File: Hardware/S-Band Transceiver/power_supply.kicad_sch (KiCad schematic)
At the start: 0 parts

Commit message: Updates to power supply schematic
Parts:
- added U14: AP2127K-3.3, Package_TO_SOT_SMD:SOT-23-5, symbol Regulator_Linear:AP2127K-3.3
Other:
- note added: "Power requirements ADF4351: 3.3V, 27+36+80+26 mA = 169 mA ADL5380: 5V, 245 mA 2 x TSS-53LNB3+: 3V, 42 mA each 2 x ADL5906: 5V, 68 mA PE44820: 3.3V, 1 mA DAT-31A+: 3.3V, 1 mA"
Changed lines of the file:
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@@
 		(rev "v1.0")
 	)
+	(text "Power requirements\nADF4351: 3.3V, 27+36+80+26 mA = 169 mA\nADL5380: 5V, 245 mA\n2 x TSS-53LNB3+: 3V, 42 mA each\n2 x ADL5906: 5V, 68 mA\nPE44820: 3.3V, 1 mA\nDAT-31A+: 3.3V, 1 mA\n\n"
+		(exclude_from_sim no)
+		(at 41.91 30.226 0)
+		(effects
+			(font
+				(size 1.27 1.27)
+			)
+			(justify left)
+		)
+	)
+	(symbol
+		(lib_id "Regulator_Linear:AP2127K-3.3")
+		(at 87.63 44.45 0)
+		(unit 1)
+		(exclude_from_sim no)
+		(in_bom yes)
+		(on_board yes)
+		(dnp no)
+		(fields_autoplaced yes)
+		(property "Reference" "U14"
+			(at 87.63 35.56 0)
+			(effects
+				(font
+					(size 1.27 1.27)
+				)
+			)
+		)
+		(property "Value" "AP2127K-3.3"
+			(at 87.63 38.1 0)
+			(effects
+				(font
+					(size 1.27 1.27)
+				)
+			)
+		)
+		(property "Footprint" "Package_TO_SOT_SMD:SOT-23-5"
+			(at 87.63 36.195 0)
+			(effects
+				(font
+					(size 1.27 1.27)
+				)
+				(hide yes)
+			)
+		)
+		(property "Datasheet" "https://www.diodes.com/assets/Datasheets/AP2127.pdf"
+			(at 87.63 41.91 0)
+			(effects
+				(font
+					(size 1.27 1.27)
+				)
+				(hide yes)
+			)
+		)
+		(property "Description" "300mA low dropout linear regulator, shutdown pin, 2.5V-6V input voltage, 3.3V fixed positive output, SOT-23-5"
+			(at 87.63 44.45 0)
+			(effects
+				(font
+					(size 1.27 1.27)
+				)
+				(hide yes)
+			)
+		)
+		(pin "1"
+		)
+		(pin "2"
+		)
+		(pin "5"
+		)
+		(pin "3"
+		)
+		(pin "4"
+		)
+		(instances
+			(project "S-Band Transceiver"
+				(path "/811f57cf-e3df-4fba-aff9-353adc85299e/39233606-ce53-49cf-9f32-d543f22663a6"
+					(reference "U14")
+					(unit 1)
+				)
+			)
+		)
+	)
 )

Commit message: Changes to schematic
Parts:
- removed U14: AP2127K-3.3, Package_TO_SOT_SMD:SOT-23-5, symbol Regulator_Linear:AP2127K-3.3
- added C40: 10uF, symbol Device:C_Polarized_Small_US
- added C41: 22uF, symbol Device:C_Polarized_Small_US
- added U14: AZ1117-3.3, Package_TO_SOT_SMD:SOT-223-3_TabPin2, symbol Regulator_Linear:AZ1117-3.3
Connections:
- new net +3V3A: C41.1, U14.2 (VO)
- new net +5V: C40.1, U14.3 (VI)
- new net GND: C40.2, C41.2, U14.1 (GND)
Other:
- note added: "B0505XT-2WR3"

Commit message: Updating schematic
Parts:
- added C4: 10uF, symbol Device:C_Polarized_Small_US
- added C5: 4.7uF, symbol Device:C_Polarized_Small_US
- added U2: IES0105S05-H, symbol _tim-DC_DC:IES0105S05-H
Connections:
- net +5V: now also C5.1, U2.2 (+Vin)
- net GND: now also C4.1, C5.2, U2.1 (-Vin), U2.5 (+Vout)
- new net -5V: C4.2, U2.4 (-Vout)
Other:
- note added: "1 Amp Max"
- note added: "200mA Max"
- note added: "B0505XT-2WR3 or IES0105S05-H"
- note removed: "B0505XT-2WR3"

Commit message: Updates to schematic
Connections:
- net +3V3A renamed +3.3VA
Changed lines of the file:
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@@
 	(wire
 		(pts
-			(xy 101.6 45.72) (xy 101.6 48.26)
+			(xy 101.6 44.45) (xy 101.6 48.26)
 		)
 		(stroke
@@
 		)
 	)
-	(global_label "+3V3A"
-		(shape input)
-		(at 101.6 45.72 90)
+	(symbol
+		(lib_id "power:+3.3VA")
+		(at 101.6 44.45 0)
+		(unit 1)
+		(exclude_from_sim no)
+		(in_bom yes)
+		(on_board yes)
+		(dnp no)
 		(fields_autoplaced yes)
-		(effects
-			(font
-				(size 1.27 1.27)
-			)
-			(justify left)
-		)
-		(property "Intersheetrefs" "${INTERSHEET_REFS}"
-			(at 101.6 36.5662 90)
+		(property "Reference" "#PWR0123"
+			(at 101.6 48.26 0)
 			(effects
 				(font
 					(size 1.27 1.27)
 				)
-				(justify left)
 				(hide yes)
 			)
 		)
+		(property "Value" "+3.3VA"
+			(at 101.6 39.37 0)
+			(effects
+				(font
+					(size 1.27 1.27)
+				)
+			)
+		)
+		(property "Footprint" ""
+			(at 101.6 44.45 0)
+			(effects
+				(font
+					(size 1.27 1.27)
+				)
+				(hide yes)
+			)
+		)
+		(property "Datasheet" ""
+			(at 101.6 44.45 0)
+			(effects
+				(font
+					(size 1.27 1.27)
+				)
+				(hide yes)
+			)
+		)
+		(property "Description" "Power symbol creates a global label with name \"+3.3VA\""
+			(at 101.6 44.45 0)
+			(effects
+				(font
+					(size 1.27 1.27)
+				)
+				(hide yes)
+			)
+		)
+		(pin "1"
+		)
+		(instances
+			(project "S-Band Transceiver"
+				(path "/811f57cf-e3df-4fba-aff9-353adc85299e/39233606-ce53-49cf-9f32-d543f22663a6"
+					(reference "#PWR0123")
+					(unit 1)
+				)
+			)
+		)

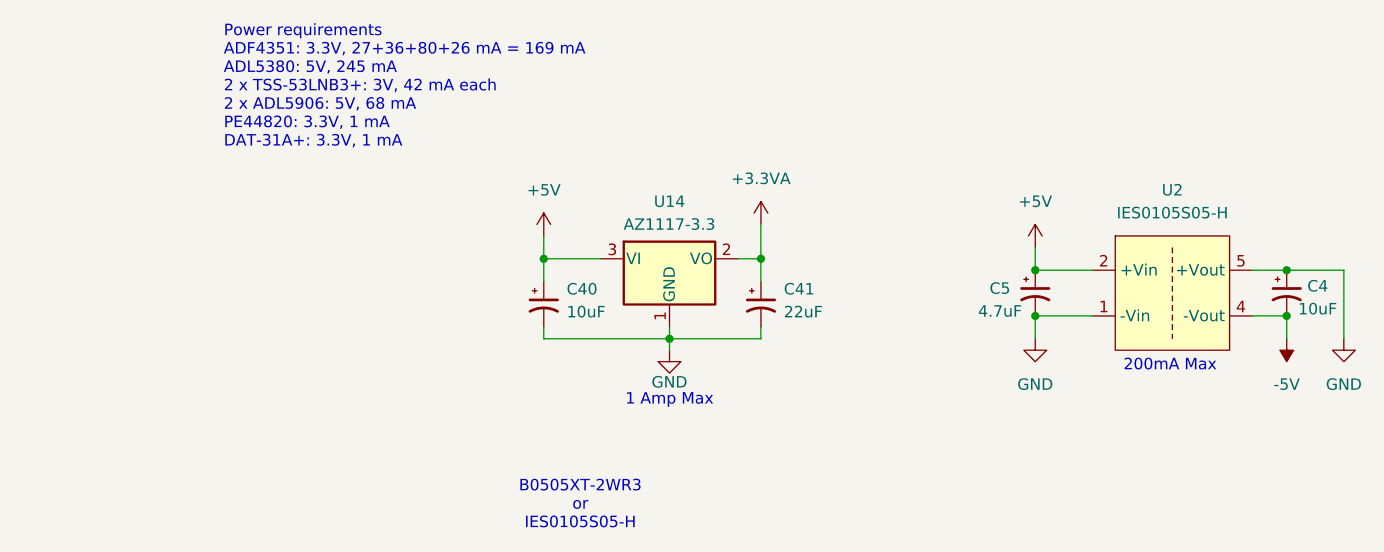
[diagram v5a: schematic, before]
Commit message: Updates to Schematic
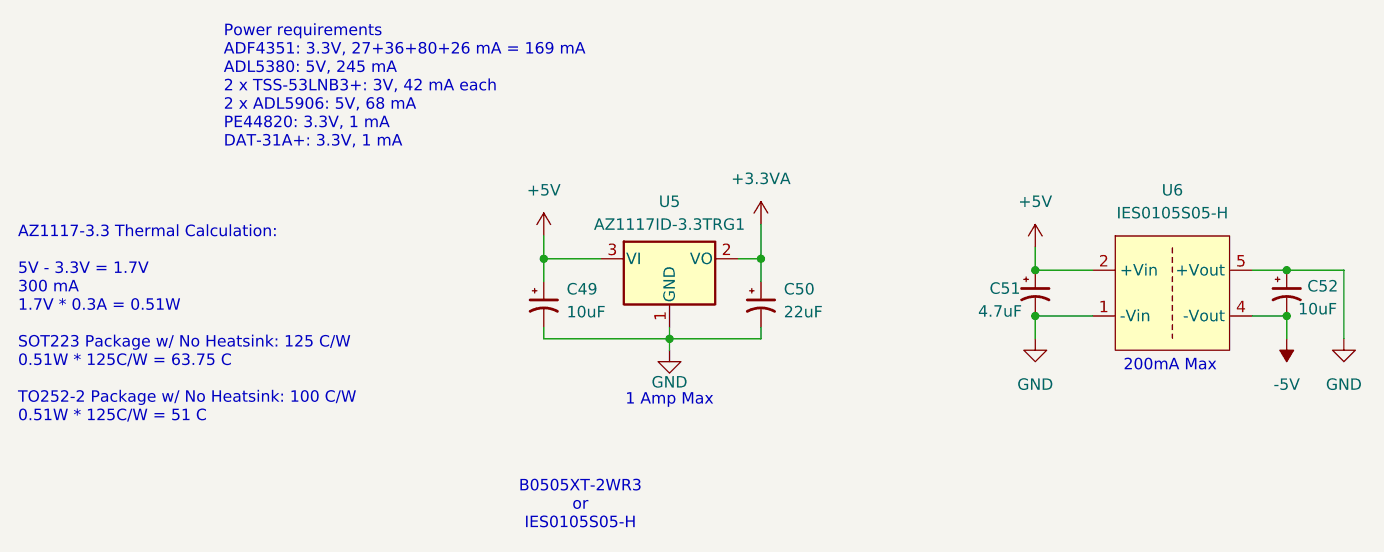
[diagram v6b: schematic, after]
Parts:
- U5: renamed from U14; value AZ1117-3.3 -> AZ1117ID-3.3TRG1; footprint Package_TO_SOT_SMD:SOT-223-3_TabPin2 -> Package_TO_SOT_SMD:TO-252-2; Digikey (none) -> AZ1117ID-3.3TRG1-ND
- U6: renamed from U2; footprint (none) -> _tim-DC-DC:IES0105S05-H; Digikey (none) -> 1470-IES0105S05-H-ND
- renumbered C40 to C49, C41 to C50, C5 to C51, C4 to C52
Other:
- note added: "AZ1117-3.3 Thermal Calculation: 5V - 3.3V = 1.7V 300 mA 1.7V * 0.3A = 0.51W SOT223 Package w/ No Heatsink: 125 C/W 0.51W * 125C/W = 63.75 C TO252-2 Package w/ No Heatsink: 100 C/W 0.51W * 125C/W = 51 C"
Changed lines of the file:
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@@
+		)
+	)
+	(text "AZ1117-3.3 Thermal Calculation:\n\n5V - 3.3V = 1.7V\n300 mA\n1.7V * 0.3A = 0.51W\n\nSOT223 Package w/ No Heatsink: 125 C/W\n0.51W * 125C/W = 63.75 C\n\nTO252-2 Package w/ No Heatsink: 100 C/W\n0.51W * 125C/W = 51 C\n"
+		(exclude_from_sim no)
+		(at 19.05 55.626 0)
+		(effects
+			(font
+				(size 1.27 1.27)
+			)
+			(justify left)
 		)
 	)
@@
 		(dnp no)
 		(fields_autoplaced yes)
-		(property "Reference" "#PWR0123"
+		(property "Reference" "#PWR067"
 			(at 101.6 48.26 0)
 			(effects
@@
 			(project "S-Band Transceiver"
 				(path "/811f57cf-e3df-4fba-aff9-353adc85299e/39233606-ce53-49cf-9f32-d543f22663a6"
-					(reference "#PWR0123")
+					(reference "#PWR067")
 					(unit 1)
 				)
@@
 		(dnp no)
 		(fields_autoplaced yes)
-		(property "Reference" "U2"
+		(property "Reference" "U6"
 			(at 147.32 40.64 0)
 			(effects
@@
 			)
 		)
-		(property "Footprint" ""
+		(property "Footprint" "_tim-DC-DC:IES0105S05-H"
 			(at 147.32 52.07 0)
 			(effects
@@
 			)
 		)
+		(property "Digikey" "1470-IES0105S05-H-ND"
+			(at 147.32 52.07 0)
+			(effects
+				(font
+					(size 1.27 1.27)
+				)
+				(hide yes)
+			)
+		)
 		(pin "5"
 		)
@@
 			(project "S-Band Transceiver"
 				(path "/811f57cf-e3df-4fba-aff9-353adc85299e/39233606-ce53-49cf-9f32-d543f22663a6"
-					(reference "U2")
+					(reference "U6")
 					(unit 1)
 				)
@@
 		(dnp no)
 		(fields_autoplaced yes)
-		(property "Reference" "U14"
+		(property "Reference" "U5"
 			(at 91.44 41.91 0)
 			(effects
@@
 			)
 		)
-		(property "Value" "AZ1117-3.3"
+		(property "Value" "AZ1117ID-3.3TRG1"
 			(at 91.44 44.45 0)
 			(effects
@@
 			)
 		)
-		(property "Footprint" "Package_TO_SOT_SMD:SOT-223-3_TabPin2"
+		(property "Footprint" "Package_TO_SOT_SMD:TO-252-2"
 			(at 91.44 41.91 0)
 			(effects
@@
 			)
 		)
+		(property "Digikey" "AZ1117ID-3.3TRG1-ND"
+			(at 91.44 48.26 0)
+			(effects
+				(font
+					(size 1.27 1.27)
+				)
+				(hide yes)
+			)
+		)
 		(pin "2"
 		)
@@
 			(project "S-Band Transceiver"
 				(path "/811f57cf-e3df-4fba-aff9-353adc85299e/39233606-ce53-49cf-9f32-d543f22663a6"
-					(reference "U14")
+					(reference "U5")
 					(unit 1)
 				)
@@
 		(dnp no)
 		(fields_autoplaced yes)
-		(property "Reference" "#PWR0106"
+		(property "Reference" "#PWR068"
 			(at 132.08 50.8 0)
 			(effects
@@
 			(project "S-Band Transceiver"
 				(path "/811f57cf-e3df-4fba-aff9-353adc85299e/39233606-ce53-49cf-9f32-d543f22663a6"
-					(reference "#PWR0106")
+					(reference "#PWR068")
 					(unit 1)
 				)
@@
 		(dnp no)
 		(fields_autoplaced yes)
-		(property "Reference" "#PWR062"
+		(property "Reference" "#PWR065"
 			(at 77.47 49.53 0)
 			(effects
@@
 			(project "S-Band Transceiver"
 				(path "/811f57cf-e3df-4fba-aff9-353adc85299e/39233606-ce53-49cf-9f32-d543f22663a6"
-					(reference "#PWR062")
+					(reference "#PWR065")
 					(unit 1)
 				)
@@
 		(on_board yes)
 		(dnp no)
-		(property "Reference" "#PWR061"
+		(property "Reference" "#PWR066"
 			(at 91.44 64.77 0)
 			(effects
@@
 			(project "S-Band Transceiver"
 				(path "/811f57cf-e3df-4fba-aff9-353adc85299e/39233606-ce53-49cf-9f32-d543f22663a6"
-					(reference "#PWR061")
+					(reference "#PWR066")
 					(unit 1)
 				)
@@
 		(dnp no)
 		(fields_autoplaced yes)
-		(property "Reference" "#PWR0105"
+		(property "Reference" "#PWR069"
 			(at 132.08 63.5 0)
 			(effects
@@
 			(project "S-Band Transceiver"
 				(path "/811f57cf-e3df-4fba-aff9-353adc85299e/39233606-ce53-49cf-9f32-d543f22663a6"
-					(reference "#PWR0105")
+					(reference "#PWR069")
 					(unit 1)
 				)
@@
 		(on_board yes)
 		(dnp no)
-		(property "Reference" "C5"
+		(property "Reference" "C51"
 			(at 127 51.562 0)
 			(effects
@@
 			(project "S-Band Transceiver"
 				(path "/811f57cf-e3df-4fba-aff9-353adc85299e/39233606-ce53-49cf-9f32-d543f22663a6"
-					(reference "C5")
+					(reference "C51")
 					(unit 1)
 				)
@@
 		(dnp no)
 		(fields_autoplaced yes)
-		(property "Reference" "C40"
+		(property "Reference" "C49"
 			(at 80.01 51.6381 0)
 			(effects
@@
 			(project "S-Band Transceiver"
 				(path "/811f57cf-e3df-4fba-aff9-353adc85299e/39233606-ce53-49cf-9f32-d543f22663a6"
-					(reference "C40")
+					(reference "C49")
 					(unit 1)
 				)
@@
 		(dnp no)
 		(fields_autoplaced yes)
-		(property "Reference" "#PWR0104"
+		(property "Reference" "#PWR070"
 			(at 160.02 53.34 0)
 			(effects
@@
 			(project "S-Band Transceiver"
 				(path "/811f57cf-e3df-4fba-aff9-353adc85299e/39233606-ce53-49cf-9f32-d543f22663a6"
-					(reference "#PWR0104")
+					(reference "#PWR070")
 					(unit 1)
 				)
@@
 		(dnp no)
 		(fields_autoplaced yes)
-		(property "Reference" "C41"
+		(property "Reference" "C50"
 			(at 104.14 51.6381 0)
 			(effects
@@
 			(project "S-Band Transceiver"
 				(path "/811f57cf-e3df-4fba-aff9-353adc85299e/39233606-ce53-49cf-9f32-d543f22663a6"
-					(reference "C41")
+					(reference "C50")
 					(unit 1)
 				)
@@
 		(dnp no)
 		(fields_autoplaced yes)
-		(property "Reference" "#PWR0103"
+		(property "Reference" "#PWR071"
 			(at 166.37 63.5 0)
 			(effects
@@
 			(project "S-Band Transceiver"
 				(path "/811f57cf-e3df-4fba-aff9-353adc85299e/39233606-ce53-49cf-9f32-d543f22663a6"
-					(reference "#PWR0103")
+					(reference "#PWR071")
 					(unit 1)
 				)
@@
 		(on_board yes)
 		(dnp no)
-		(property "Reference" "C4"
+		(property "Reference" "C52"
 			(at 162.306 51.308 0)
 			(effects
@@
 			(project "S-Band Transceiver"
 				(path "/811f57cf-e3df-4fba-aff9-353adc85299e/39233606-ce53-49cf-9f32-d543f22663a6"
-					(reference "C4")
-					(unit 1)
-				)
+					(reference "C52")
+					(unit 1)
+				)

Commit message: Finished assigning footprints and starting board layout
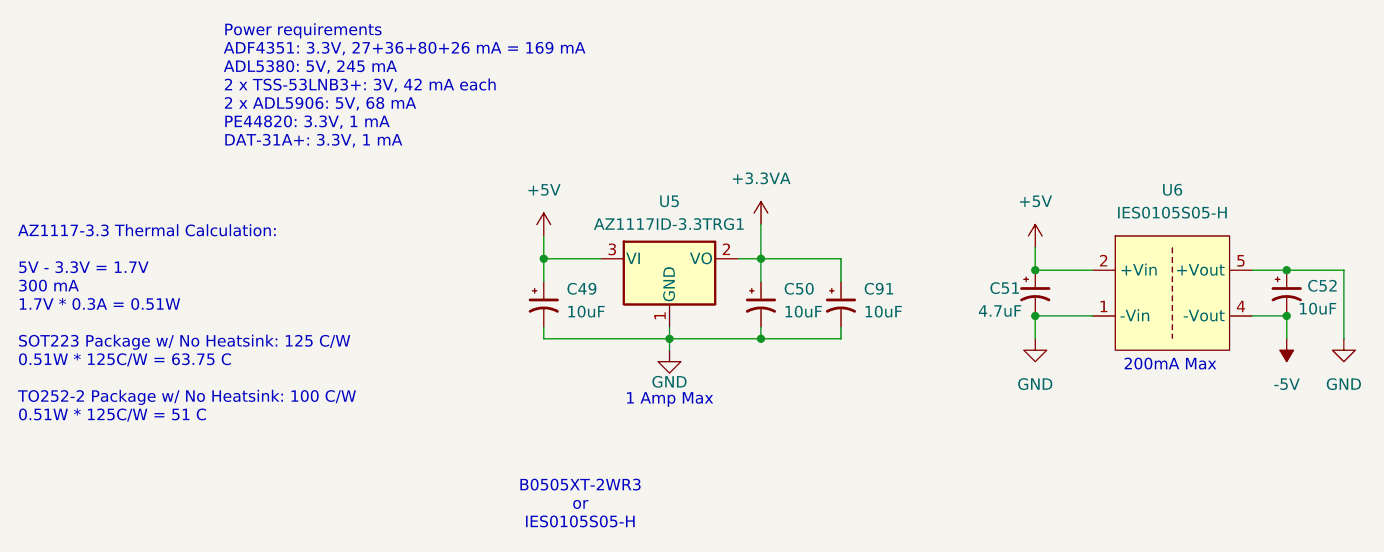
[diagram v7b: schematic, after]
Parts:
- added C91: 10uF, Capacitor_Tantalum_SMD:CP_EIA-3216-18_Kemet-A, symbol Device:C_Polarized_Small_US
- C49, C51, C52: footprint (none) -> Capacitor_Tantalum_SMD:CP_EIA-3216-18_Kemet-A
- C50: value 22uF -> 10uF; footprint (none) -> Capacitor_Tantalum_SMD:CP_EIA-3216-18_Kemet-A
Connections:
- net +3.3VA: now also C91.1
- net GND: now also C91.2
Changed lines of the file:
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@@
+	)
+	(junction
+		(at 101.6 57.15)
+		(diameter 0)
+		(color 0 0 0 0)
 	)
 	(junction
@@
 	(wire
 		(pts
+			(xy 110.49 48.26) (xy 101.6 48.26)
+		)
+		(stroke
+			(width 0)
+			(type default)
+		)
+	)
+	(wire
+		(pts
 			(xy 156.21 49.53) (xy 160.02 49.53)
 		)
@@
 	(wire
 		(pts
+			(xy 110.49 55.88) (xy 110.49 57.15)
+		)
+		(stroke
+			(width 0)
+			(type default)
+		)
+	)
+	(wire
+		(pts
 			(xy 77.47 48.26) (xy 77.47 50.8)
 		)
@@
 		(pts
 			(xy 101.6 55.88) (xy 101.6 57.15)
+		)
+		(stroke
+			(width 0)
+			(type default)
+		)
+	)
+	(wire
+		(pts
+			(xy 110.49 50.8) (xy 110.49 48.26)
+		)
+		(stroke
+			(width 0)
+			(type default)
+		)
+	)
+	(wire
+		(pts
+			(xy 110.49 57.15) (xy 101.6 57.15)
 		)
 		(stroke
@@
 			)
 		)
-		(property "Footprint" ""
+		(property "Footprint" "Capacitor_Tantalum_SMD:CP_EIA-3216-18_Kemet-A"
 			(at 132.08 52.07 0)
 			(effects
@@
 	(symbol
 		(lib_id "Device:C_Polarized_Small_US")
+		(at 101.6 53.34 0)
+		(unit 1)
+		(exclude_from_sim no)
+		(in_bom yes)
+		(on_board yes)
+		(dnp no)
+		(fields_autoplaced yes)
+		(property "Reference" "C50"
+			(at 104.14 51.6381 0)
+			(effects
+				(font
+					(size 1.27 1.27)
+				)
+				(justify left)
+			)
+		)
+		(property "Value" "10uF"
+			(at 104.14 54.1781 0)
+			(effects
+				(font
+					(size 1.27 1.27)
+				)
+				(justify left)
+			)
+		)
+		(property "Footprint" "Capacitor_Tantalum_SMD:CP_EIA-3216-18_Kemet-A"
+			(at 101.6 53.34 0)
+			(effects
+				(font
+					(size 1.27 1.27)
+				)
+				(hide yes)
+			)
+		)
+		(property "Datasheet" "~"
+			(at 101.6 53.34 0)
+			(effects
+				(font
+					(size 1.27 1.27)
+				)
+				(hide yes)
+			)
+		)
+		(property "Description" "Polarized capacitor, small US symbol"
+			(at 101.6 53.34 0)
+			(effects
+				(font
+					(size 1.27 1.27)
+				)
+				(hide yes)
+			)
+		)
+		(pin "2"
+		)
+		(pin "1"
+		)
+		(instances
+			(project "S-Band Transceiver"
+				(path "/811f57cf-e3df-4fba-aff9-353adc85299e/39233606-ce53-49cf-9f32-d543f22663a6"
+					(reference "C50")
+					(unit 1)
+				)
+			)
+		)
+	)
+	(symbol
+		(lib_id "Device:C_Polarized_Small_US")
 		(at 77.47 53.34 0)
 		(unit 1)
@@
 			)
 		)
-		(property "Footprint" ""
+		(property "Footprint" "Capacitor_Tantalum_SMD:CP_EIA-3216-18_Kemet-A"
 			(at 77.47 53.34 0)
 			(effects
@@
 	(symbol
 		(lib_id "Device:C_Polarized_Small_US")
-		(at 101.6 53.34 0)
+		(at 110.49 53.34 0)
 		(unit 1)
 		(exclude_from_sim no)
@@
 		(dnp no)
 		(fields_autoplaced yes)
-		(property "Reference" "C50"
-			(at 104.14 51.6381 0)
+		(property "Reference" "C91"
+			(at 113.03 51.6381 0)
 			(effects
 				(font
@@
 			)
 		)
-		(property "Value" "22uF"
-			(at 104.14 54.1781 0)
+		(property "Value" "10uF"
+			(at 113.03 54.1781 0)
 			(effects
 				(font
@@
 			)
 		)
-		(property "Footprint" ""
-			(at 101.6 53.34 0)
+		(property "Footprint" "Capacitor_Tantalum_SMD:CP_EIA-3216-18_Kemet-A"
+			(at 110.49 53.34 0)
 			(effects
 				(font
@@
 		)
 		(property "Datasheet" "~"
-			(at 101.6 53.34 0)
+			(at 110.49 53.34 0)
 			(effects
 				(font
@@
 		)
 		(property "Description" "Polarized capacitor, small US symbol"
-			(at 101.6 53.34 0)
+			(at 110.49 53.34 0)
 			(effects
 				(font
@@
 			(project "S-Band Transceiver"
 				(path "/811f57cf-e3df-4fba-aff9-353adc85299e/39233606-ce53-49cf-9f32-d543f22663a6"
-					(reference "C50")
+					(reference "C91")
 					(unit 1)
 				)
@@
 			)
 		)
-		(property "Footprint" ""
+		(property "Footprint" "Capacitor_Tantalum_SMD:CP_EIA-3216-18_Kemet-A"
 			(at 160.02 52.07 0)
 			(effects
